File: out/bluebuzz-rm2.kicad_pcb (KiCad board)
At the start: 6 copper layers, 28 x 44 mm, 109 parts, among them J1 USB-C, J2 BAT, J3 SWD, J4 MOT, J5 TP, J6 PROBE, Q1 AO3400A, Q2 AO3400A, Q3 2N7002, SW1 PWR, U1 RP2350A, U10 USBLC6-2P6, U11 TPS22918DBVR, U2 BQ24074RGT, U20 DPS368, U21 DPS368, U22 DPS368, U23 DPS368, U24 DPS368, U3 TLV75533PDBV, U30 LSM6DS3TR-C, U5 TPS22918DBVR, U6 W25Q32JVUUIQ, U7 RM2, Y1 12MHz

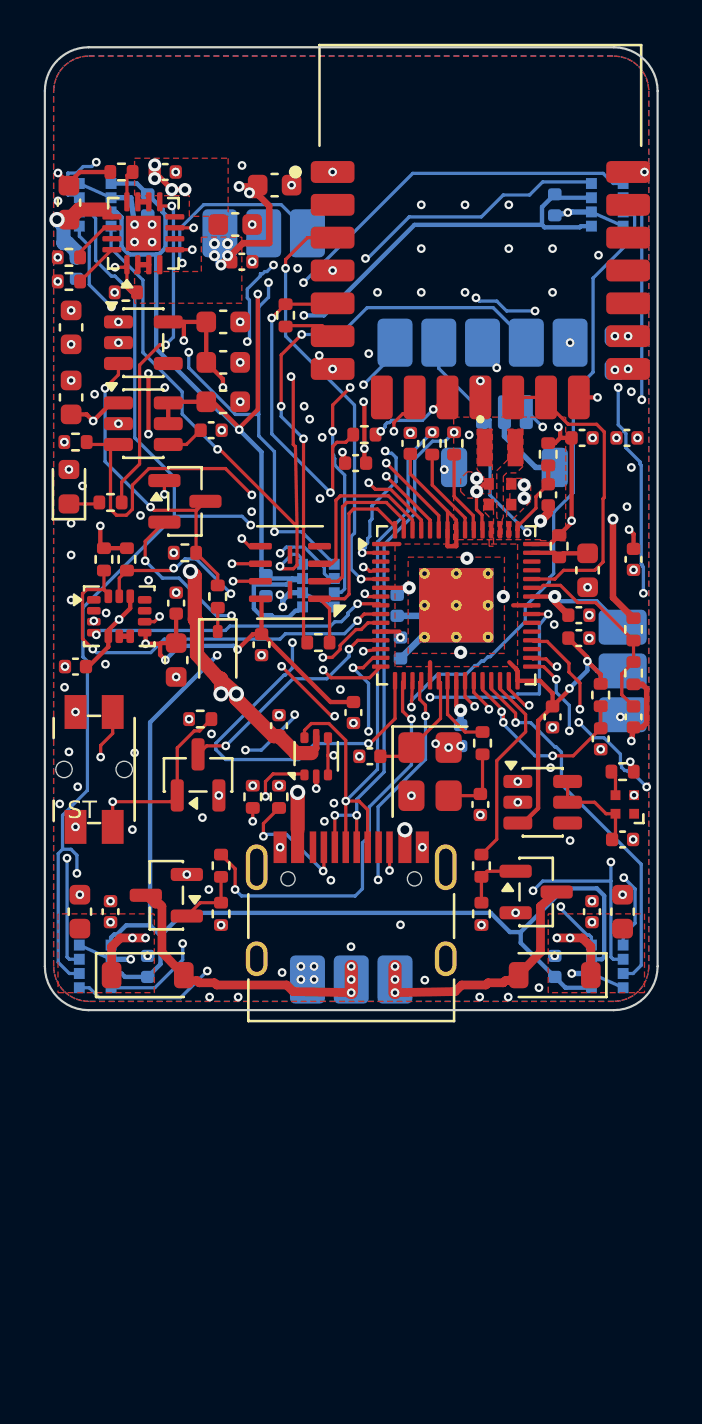
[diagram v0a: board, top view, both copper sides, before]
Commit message: Configure GitHub Pages, add Pages link to README, export STEP without copper
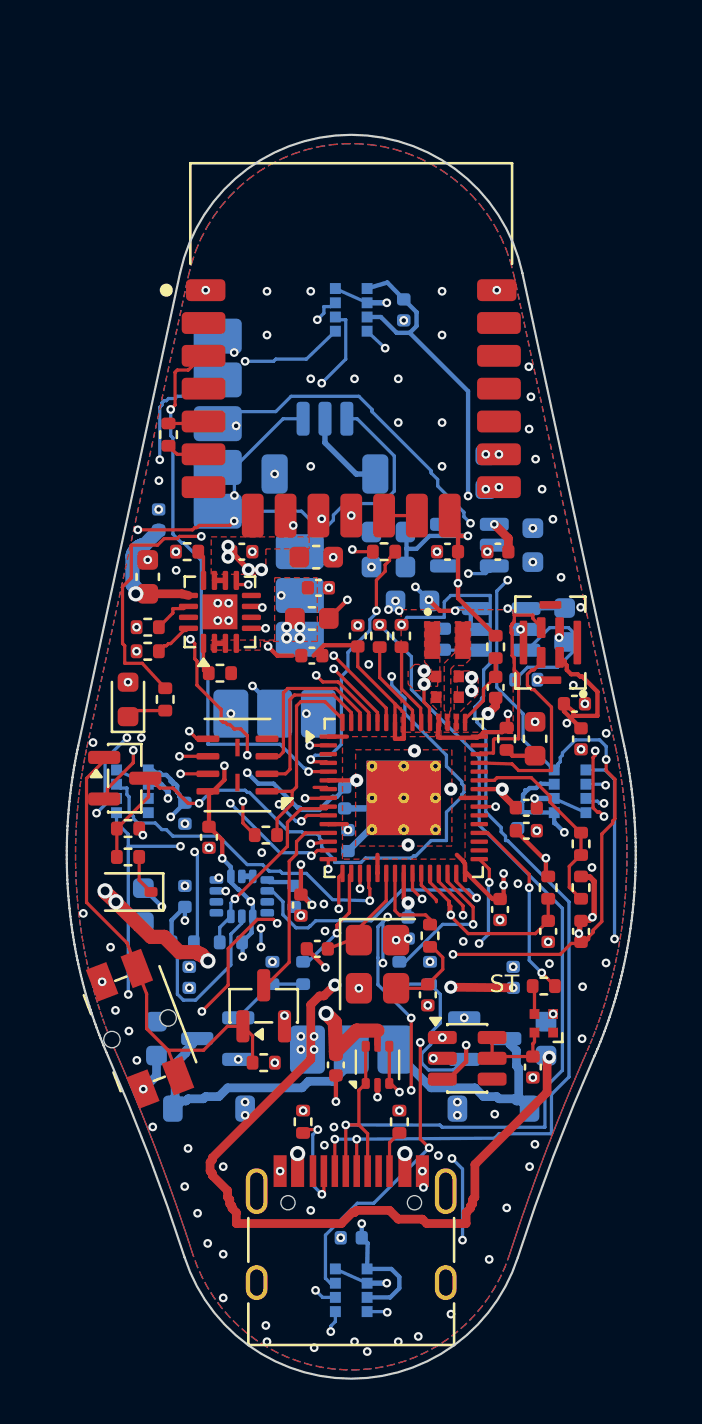
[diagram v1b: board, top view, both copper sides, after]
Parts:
- removed C124: 100n, Capacitor_SMD:C_0402_1005Metric
- removed U24: DPS368, bluebuzz-rm2:DPS368_LGA-8
- added C140: 100n, Capacitor_SMD:C_0402_1005Metric, F.Cu at (110.2, 108.0)
- added U40: MP34DT05-A, bluebuzz-rm2:MP34DT05_HCLGA-4, F.Cu at (109.1, 105.2)
- C130, C131, C132, C20, C21, C22, C40, C41, C42, C43, C50, C51, C52, D3, D4, Q1, Q2, R130, R131, R40, R41, R42, R43, R50, U3, U30, U5: moved to B.Cu
- moved C121 28.1 mm to (107.6, 113.2)
- moved U21 26.9 mm to (110.0, 112.0)
- moved C51 24.8 mm to (109.8, 104.4), turned to -90 degrees
- moved C20 23.3 mm to (108.3, 100.8)
- moved R50 23.3 mm to (108.0, 106.9), turned to 0 degrees
- moved C12 19.9 mm to (98.2, 104.1)
- moved U23 18.9 mm to (100.0, 134.8), turned to 180 degrees
- moved U5 18.9 mm to (106.8, 104.6), turned to 180 degrees
- moved R130 18.4 mm to (94.5, 118.9), turned to 180 degrees
- moved R13 17.9 mm to (94.0, 106.6), turned to 0 degrees
- moved C14 17.7 mm to (95.0, 101.0)
- moved R131 17.7 mm to (92.3, 118.9), turned to 0 degrees
- moved U2 17.7 mm to (94.0, 103.8)
- moved R11 17.6 mm to (92.5, 101.0)
- moved U3 17.5 mm to (105.4, 100.8), turned to 180 degrees
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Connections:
- U1 pad 32: TAC_CS5 -> (no net)
- U1 pad 42: (no net) -> PDM_DATA
- U1 pad 43: (no net) -> PDM_CLK
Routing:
- net TAC_CS5: track 54.6 -> 0.00 mm, vias 9 -> 0
- net 3V3_SENS: track 126.8 -> 82.5 mm, vias 4 -> 7
- net VBAT: track 42.2 -> 0.55 mm, vias 8 -> 4
- net VSYS: track 9.05 -> 48.9 mm, vias 25 -> 27
- net TAC_SDO: track 109.0 -> 75.7 mm, vias 10 -> 12
- net LDO_EN: track 14.3 -> 37.8 mm, vias 2 -> 3
- net TAC_SDI: track 124.4 -> 103.5 mm, vias 7 -> 10
- net 3V3_SYS: track 125.7 -> 105.1 mm, vias 19 -> 18
- net RUN: track 29.8 -> 50.0 mm, vias 4 -> 5
- net SWDIO: track 35.8 -> 16.0 mm, vias 3 -> 0
- net USB_DM: track 34.7 -> 54.2 mm
- net PG_N: track 30.6 -> 15.3 mm
- net TAC_CS3: track 30.9 -> 15.7 mm, vias 3 -> 1
- net TAC_CS2: track 29.4 -> 15.4 mm, vias 1 -> 2
- net MOTOR1_PWM: track 18.6 -> 5.09 mm, vias 2 -> 1
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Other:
- board size 28 x 44 mm -> 26 x 56.8 mm
- board text added: "PROBE"
- board text removed: "PROBE SC GND SD"

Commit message: Complete routing on 2.0mm inward-offset squish outline (0 DRC errors, 0 unconnected, audit clean) and update exports/site
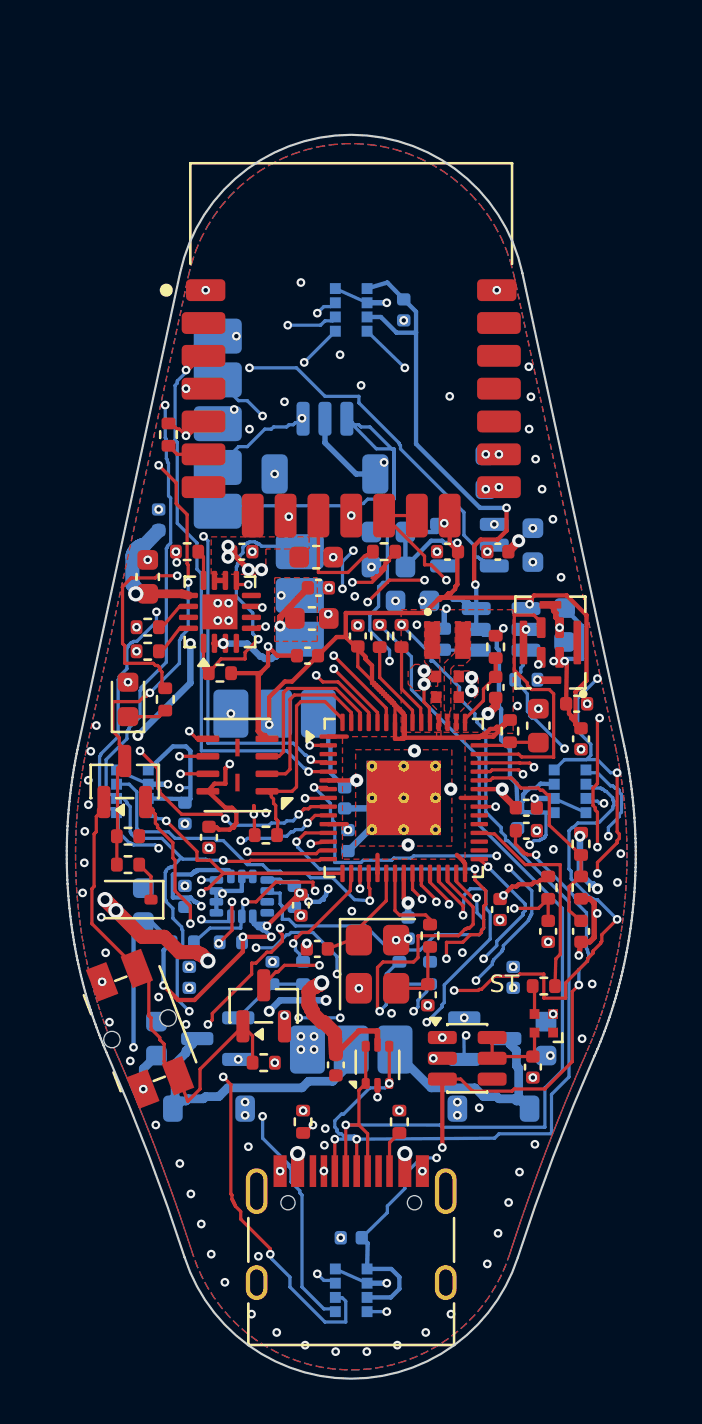
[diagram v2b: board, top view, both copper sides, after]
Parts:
- moved C85 0.62 mm to (108.5, 109.0)
- moved R85 0.38 mm to (107.2, 109.2)
- moved D6 0.35 mm to (89.8, 117.0)
- moved R63 0.35 mm to (89.8, 114.0)
- moved R66 0.35 mm to (89.8, 115.3)
- moved C91 0.20 mm to (98.0, 105.8)
- moved D5 0.15 mm to (89.7, 111.5), turned to 90 degrees
- moved C140 0.10 mm to (110.3, 108.0)
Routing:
- net 3V3_SYS: track 105.1 -> 185.3 mm, vias 18 -> 22
- net VBAT: track 0.55 -> 52.0 mm, vias 4 -> 8
- net VSYS: track 48.9 -> 6.99 mm, vias 27 -> 26
- net SWDIO: track 16.0 -> 44.3 mm, vias 0 -> 2
- net TAC_SDO: track 75.7 -> 97.6 mm, vias 12 -> 7
- net WL_DATA: track 14.0 -> 34.9 mm, vias 2 -> 4
- net SENS_EN: track 7.70 -> 27.7 mm, vias 0 -> 3
- net 3V3_SENS: track 82.5 -> 100.0 mm, vias 7 -> 10
- net WL_ON: track 1.50 -> 18.3 mm, vias 0 -> 2
- net BTN: track 8.87 -> 25.0 mm, vias 0 -> 4
- net SDA: track 8.93 -> 24.7 mm, vias 1 -> 6
- net TS: track 1.53 -> 12.3 mm, vias 0 -> 1
- net TAC_SCK: track 103.2 -> 93.9 mm, vias 7 -> 8
- net SWCLK: track 33.4 -> 42.3 mm
- net BOOTSEL: track 25.6 -> 34.3 mm, vias 2 -> 4
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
